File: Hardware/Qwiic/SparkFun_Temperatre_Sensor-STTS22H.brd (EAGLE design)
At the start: 25.4 x 25.4 mm, 54 parts, among them J1 QWIIC_RIGHT_ANGLE, J2 QWIIC_RIGHT_ANGLE, U2 STTS22H

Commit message: Moves OSHW logo, approves various DRC errors, moves silk
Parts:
- moved LOGO2 21.2 mm to (4.47, 5.95)
- moved U$6 3.18 mm to (17.8, 13.6)
- moved U$8 2.93 mm to (6.25, 13.7)
- moved U$19 0.13 mm to (16.6, 18.0)
- moved U$22 0.13 mm to (7.98, 18.0)
- moved U$25 0.13 mm to (12.7, 6.86)
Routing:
- net 3.3V: vias 5 -> 3
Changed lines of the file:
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@@
 <attribute name="REV" value="" x="-19.05" y="-16.51" size="1.778" layer="27" display="off"/>
 </element>
-<element name="LOGO2" library="SparkFun-Aesthetics" package="OSHW-LOGO-MINI" value="OSHW-LOGOMINI" x="23.7744" y="14.71295" smashed="yes" rot="MR0"/>
+<element name="LOGO2" library="SparkFun-Aesthetics" package="OSHW-LOGO-MINI" value="OSHW-LOGOMINI" x="4.4704" y="5.94995" smashed="yes" rot="MR0"/>
 <element name="STANDOFF1" library="SparkFun-Hardware" package="STAND-OFF-TIGHT" value="STAND-OFFTIGHT" x="2.54" y="22.86" smashed="yes"/>
 <element name="STANDOFF2" library="SparkFun-Hardware" package="STAND-OFF-TIGHT" value="STAND-OFFTIGHT" x="2.54" y="2.54" smashed="yes"/>
@@
 </element>
 <element name="U$16" library="bot" package="#LED#11" value="" x="23.622" y="16.9926" smashed="yes" rot="MR0"/>
-<element name="U$25" library="bot" package="#I2C#11" value="" x="12.7" y="6.985" smashed="yes" rot="MR0"/>
+<element name="U$25" library="bot" package="#I2C#11" value="" x="12.7" y="6.858" smashed="yes" rot="MR0"/>
 <element name="U$1" library="top" package="#GND#3" value="" x="7.62" y="3.937" smashed="yes" rot="R90"/>
 <element name="U$2" library="top" package="#3V3#4" value="" x="10.16" y="3.81" smashed="yes" rot="R90"/>
@@
 <attribute name="VALUE" value="15k" x="13.462" y="17.78" size="0.6096" layer="27" font="vector" ratio="20" rot="R90" align="top-center"/>
 </element>
-<element name="U$6" library="top" package="#ADDR#6" value="" x="17.78" y="16.8148" smashed="yes" rot="MR0"/>
+<element name="U$6" library="top" package="#ADDR#6" value="" x="17.78" y="13.6398" smashed="yes" rot="MR0"/>
 <element name="U2" library="STTS22H" package="UDFN-6L" value="STTS22H" x="12.7" y="12.7" smashed="yes">
 <attribute name="NAME" x="12.041" y="14.96833125" size="0.6096" layer="25" font="vector" ratio="20"/>
@@
 <element name="U$5" library="top" package="#SDA#7" value="" x="12.7" y="3.9116" smashed="yes" rot="MR270"/>
 <element name="U$7" library="top" package="#SCL#6" value="" x="15.24" y="3.7592" smashed="yes" rot="MR270"/>
-<element name="U$8" library="top" package="#ADDR1#9" value="" x="6.5024" y="16.5862" smashed="yes" rot="MR0"/>
+<element name="U$8" library="top" package="#ADDR1#9" value="" x="6.2484" y="13.6652" smashed="yes" rot="MR0"/>
 <element name="U$12" library="top" package="#0X3C#25" value="" x="14.4272" y="15.3416" smashed="yes" rot="MR0"/>
 <element name="U$13" library="top" package="#0X3E#25" value="" x="21.1836" y="15.3416" smashed="yes" rot="MR0"/>
@@
 <element name="U$15" library="top" package="#0X38#25" value="" x="3.2512" y="15.2908" smashed="yes" rot="MR0"/>
 <element name="U$17" library="top" package="TEMPERATURE23" value="" x="12.7" y="19.6088" smashed="yes" rot="MR0"/>
-<element name="U$19" library="top" package="SENSOR24" value="" x="16.6116" y="18.0848" smashed="yes" rot="MR0"/>
-<element name="U$22" library="top" package="STTS22H21" value="" x="7.9756" y="18.0848" smashed="yes" rot="MR0"/>
+<element name="U$19" library="top" package="SENSOR24" value="" x="16.6116" y="17.9578" smashed="yes" rot="MR0"/>
+<element name="U$22" library="top" package="STTS22H21" value="" x="7.9756" y="17.9578" smashed="yes" rot="MR0"/>
 <element name="U$23" library="top" package="TEMPERATURE23" value="" x="12.7" y="24.13" smashed="yes"/>
 <element name="U$24" library="top" package="SENSOR24" value="" x="12.7" y="22.5552" smashed="yes"/>
@@
 <wire x1="12.7" y1="6.985" x2="12.7" y2="8.382" width="0.4064" layer="16"/>
 <wire x1="10.16" y1="8.1534" x2="11.3284" y2="6.985" width="0.4064" layer="1"/>
-<via x="11.176" y="11.176" extent="1-16" drill="0.3048"/>
 <polygon width="0.127" layer="1" thermals="no">
 <vertex x="11.8364" y="11.938"/>
@@
 <wire x1="6.612" y1="13.2" x2="7.6572" y2="12.1548" width="0.4064" layer="1"/>
 <wire x1="15.24" y1="18.63" x2="12.7" y2="18.63" width="0.4064" layer="1"/>
-<via x="19.1596" y="12.2" extent="1-16" drill="0.3048"/>
 <wire x1="5.588" y1="15.1892" x2="5.5372" y2="15.24" width="0.4064" layer="16"/>
 <wire x1="5.08" y1="13.2" x2="3.945" y2="13.2" width="0.4064" layer="1"/>

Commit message: Moves address jumper for better symmetry
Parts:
- moved U$13 1.27 mm to (22.5, 15.3)
- moved U$12 1.27 mm to (15.7, 15.3)
- moved ADDR 1.27 mm to (19.1, 15.2)
- moved U$6 1.27 mm to (19.1, 13.6)
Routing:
- net ADDR: track 22.9 -> 25.3 mm
- net N$4: track 5.18 -> 6.32 mm
- net N$7: track 5.19 -> 6.22 mm
- net GND: vias 37 -> 39
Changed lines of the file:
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@@
 <setting verticaltext="up"/>
 </settings>
-<grid distance="0.05" unitdist="inch" unit="inch" style="dots" multiple="1" display="yes" altdistance="0.005" altunitdist="inch" altunit="inch"/>
+<grid distance="0.05" unitdist="inch" unit="inch" style="dots" multiple="1" display="yes" altdistance="0.001" altunitdist="inch" altunit="inch"/>
 <layers>
 <layer number="1" name="Top" color="4" fill="1" visible="yes" active="yes"/>
@@
 <attribute name="VALUE" x="6.35" y="-0.762" size="0.6096" layer="27" font="vector" ratio="20"/>
 </element>
-<element name="ADDR" library="SparkFun-Jumpers" package="SMT-JUMPER_3_1-NC_TRACE_SILK" package3d_urn="urn:adsk.eagle:package:39288/1" value="JUMPER-SMT_3_1-NC_TRACE_SILK" x="17.78" y="15.24" smashed="yes" rot="MR0">
-<attribute name="NAME" x="17.78" y="16.383" size="0.6096" layer="26" font="vector" ratio="20" rot="MR0" align="bottom-center"/>
-<attribute name="VALUE" x="17.78" y="14.097" size="0.6096" layer="28" font="vector" ratio="20" rot="MR0" align="top-center"/>
+<element name="ADDR" library="SparkFun-Jumpers" package="SMT-JUMPER_3_1-NC_TRACE_SILK" package3d_urn="urn:adsk.eagle:package:39288/1" value="JUMPER-SMT_3_1-NC_TRACE_SILK" x="19.05" y="15.24" smashed="yes" rot="MR0">
+<attribute name="NAME" x="19.05" y="16.383" size="0.6096" layer="26" font="vector" ratio="20" rot="MR0" align="bottom-center"/>
+<attribute name="VALUE" x="19.05" y="14.097" size="0.6096" layer="28" font="vector" ratio="20" rot="MR0" align="top-center"/>
 </element>
 <element name="R7" library="SparkFun-Resistors" package="0603" value="56k" x="15.24" y="17.78" smashed="yes" rot="R270">
@@
 <attribute name="VALUE" value="15k" x="13.462" y="17.78" size="0.6096" layer="27" font="vector" ratio="20" rot="R90" align="top-center"/>
 </element>
-<element name="U$6" library="top" package="#ADDR#6" value="" x="17.78" y="13.6398" smashed="yes" rot="MR0"/>
+<element name="U$6" library="top" package="#ADDR#6" value="" x="19.05" y="13.6398" smashed="yes" rot="MR0"/>
 <element name="U2" library="STTS22H" package="UDFN-6L" value="STTS22H" x="12.7" y="12.7" smashed="yes">
 <attribute name="NAME" x="12.041" y="14.96833125" size="0.6096" layer="25" font="vector" ratio="20"/>
@@
 <element name="U$7" library="top" package="#SCL#6" value="" x="15.24" y="3.7592" smashed="yes" rot="MR270"/>
 <element name="U$8" library="top" package="#ADDR1#9" value="" x="6.2484" y="13.6652" smashed="yes" rot="MR0"/>
-<element name="U$12" library="top" package="#0X3C#25" value="" x="14.4272" y="15.3416" smashed="yes" rot="MR0"/>
-<element name="U$13" library="top" package="#0X3E#25" value="" x="21.1836" y="15.3416" smashed="yes" rot="MR0"/>
+<element name="U$12" library="top" package="#0X3C#25" value="" x="15.6972" y="15.3416" smashed="yes" rot="MR0"/>
+<element name="U$13" library="top" package="#0X3E#25" value="" x="22.4536" y="15.3416" smashed="yes" rot="MR0"/>
 <element name="U$14" library="top" package="#0X3F#25" value="" x="9.5504" y="15.2908" smashed="yes" rot="MR0"/>
 <element name="U$15" library="top" package="#0X38#25" value="" x="3.2512" y="15.2908" smashed="yes" rot="MR0"/>
@@
 <via x="9.8044" y="5.8928" extent="1-16" drill="0.3048"/>
 <via x="17.9324" y="7.9756" extent="1-16" drill="0.3048"/>
-<via x="20.32" y="16.51" extent="1-16" drill="0.3048"/>
+<via x="20.1422" y="17.1704" extent="1-16" drill="0.3048"/>
 <contactref element="C1" pad="2"/>
 <via x="17.78" y="19.304" extent="1-16" drill="0.3048"/>
@@
 <via x="23.3172" y="11.0236" extent="1-16" drill="0.3048"/>
 <via x="13.716" y="17.3736" extent="1-16" drill="0.3048"/>
-<via x="16.51" y="17.653" extent="1-16" drill="0.3048"/>
-<via x="6.604" y="14.0462" extent="1-16" drill="0.3048"/>
+<via x="16.5354" y="17.7038" extent="1-16" drill="0.3048"/>
+<via x="8.1788" y="14.5542" extent="1-16" drill="0.3048"/>
+<via x="3.8608" y="14.224" extent="1-16" drill="0.3048"/>
+<via x="7.1628" y="16.6878" extent="1-16" drill="0.3048"/>
 </signal>
 <signal name="3.3V">
@@
 <wire x1="6.612" y1="13.2" x2="7.6572" y2="12.1548" width="0.4064" layer="1"/>
 <wire x1="15.24" y1="18.63" x2="12.7" y2="18.63" width="0.4064" layer="1"/>
-<wire x1="5.588" y1="15.1892" x2="5.5372" y2="15.24" width="0.4064" layer="16"/>
 <wire x1="5.08" y1="13.2" x2="3.945" y2="13.2" width="0.4064" layer="1"/>
 <wire x1="3.945" y1="13.2" x2="3.937" y2="13.208" width="0.4064" layer="1"/>
@@
 <contactref element="U2" pad="P2"/>
 <contactref element="R3" pad="1"/>
-<wire x1="9.375" y1="12.684" x2="9.359" y2="12.7" width="0.2032" layer="1"/>
 <wire x1="9.315" y1="12.744" x2="8.509" y2="13.55" width="0.2032" layer="1"/>
 <wire x1="8.509" y1="13.55" x2="7.5556" y2="13.55" width="0.2032" layer="1"/>
@@
 <contactref element="R8" pad="1"/>
 <wire x1="12.7" y1="16.93" x2="12.993" y2="16.637" width="0.2032" layer="1"/>
-<wire x1="12.993" y1="16.637" x2="13.97" y2="16.637" width="0.2032" layer="1"/>
-<via x="13.97" y="16.637" extent="1-16" drill="0.3048"/>
-<wire x1="13.97" y1="16.637" x2="13.97" y2="15.875" width="0.2032" layer="16"/>
-<wire x1="14.605" y1="15.24" x2="16.7386" y2="15.24" width="0.2032" layer="16"/>
-<wire x1="13.97" y1="15.875" x2="14.605" y2="15.24" width="0.2032" layer="16"/>
+<wire x1="12.993" y1="16.637" x2="13.7414" y2="16.637" width="0.2032" layer="1"/>
+<via x="13.7414" y="16.637" extent="1-16" drill="0.3048"/>
+<wire x1="13.7414" y1="16.637" x2="13.7414" y2="16.1036" width="0.2032" layer="16"/>
+<wire x1="14.605" y1="15.24" x2="18.0086" y2="15.24" width="0.2032" layer="16"/>
+<wire x1="13.7414" y1="16.1036" x2="14.605" y2="15.24" width="0.2032" layer="16"/>
 </signal>
 <signal name="N$7">
 <contactref element="ADDR" pad="1"/>
 <contactref element="R7" pad="2"/>
-<wire x1="18.9484" y1="15.367" x2="18.8214" y2="15.24" width="0.2032" layer="16"/>
 <wire x1="15.24" y1="16.93" x2="16.344" y2="16.93" width="0.2032" layer="1"/>
 <wire x1="16.344" y1="16.93" x2="16.383" y2="16.891" width="0.2032" layer="1"/>
 <via x="16.383" y="16.891" extent="1-16" drill="0.3048"/>
-<wire x1="16.383" y1="16.891" x2="18.415" y2="16.891" width="0.2032" layer="16"/>
-<wire x1="18.8214" y1="16.4846" x2="18.8214" y2="15.24" width="0.2032" layer="16"/>
-<wire x1="18.415" y1="16.891" x2="18.8214" y2="16.4846" width="0.2032" layer="16"/>
+<wire x1="19.589621875" y1="16.891" x2="16.383" y2="16.891" width="0.2032" layer="16"/>
+<wire x1="20.0914" y1="15.24" x2="20.0914" y2="16.389221875" width="0.2032" layer="16"/>
+<wire x1="20.0914" y1="16.389221875" x2="19.589621875" y2="16.891" width="0.2032" layer="16"/>
 </signal>
 <signal name="ADDR">
@@
 <wire x1="13.594" y1="12.065" x2="14.3336" y2="12.065" width="0.2032" layer="1"/>
 <via x="14.3336" y="12.065" extent="1-16" drill="0.3048"/>
-<wire x1="17.78" y1="12.7" x2="17.78" y2="15.24" width="0.2032" layer="16"/>
-<wire x1="14.3336" y1="12.065" x2="17.145" y2="12.065" width="0.2032" layer="16"/>
-<wire x1="17.145" y1="12.065" x2="17.78" y2="12.7" width="0.2032" layer="16"/>
-<wire x1="17.78" y1="15.24" x2="17.78" y2="16.256" width="0.2032" layer="16"/>
-<wire x1="17.78" y1="16.256" x2="17.653" y2="16.383" width="0.2032" layer="16"/>
-<wire x1="17.653" y1="16.383" x2="14.986" y2="16.383" width="0.2032" layer="16"/>
+<wire x1="18.6944" y1="16.383" x2="14.986" y2="16.383" width="0.2032" layer="16"/>
 <wire x1="14.986" y1="16.383" x2="14.605" y2="16.764" width="0.2032" layer="16"/>
 <wire x1="6.35" y1="17.145" x2="6.35" y2="15.24" width="0.2032" layer="16"/>
@@
 <wire x1="14.351" y1="17.907" x2="7.112" y2="17.907" width="0.2032" layer="16"/>
 <wire x1="7.112" y1="17.907" x2="6.35" y2="17.145" width="0.2032" layer="16"/>
+<wire x1="19.05" y1="16.0274" x2="19.05" y2="15.24" width="0.2032" layer="16"/>
+<wire x1="18.6944" y1="16.383" x2="19.05" y2="16.0274" width="0.2032" layer="16"/>
+<wire x1="18.4404" y1="12.065" x2="19.0627" y2="12.6873" width="0.2032" layer="16"/>
+<wire x1="14.3336" y1="12.065" x2="18.4404" y2="12.065" width="0.2032" layer="16"/>
+<wire x1="19.05" y1="15.24" x2="19.0627" y2="15.2273" width="0.2032" layer="16"/>
+<wire x1="19.0627" y1="15.2273" x2="19.0627" y2="12.6873" width="0.2032" layer="16"/>
 </signal>
 <signal name="SCL">
@@
 <contactref element="J2" pad="4"/>
 <contactref element="J3" pad="4"/>
-<wire x1="19.328" y1="14.2" x2="20.2946" y2="14.2" width="0.2032" layer="1"/>
+<wire x1="17.931" y1="14.2" x2="20.2946" y2="14.2" width="0.2032" layer="1"/>
 <wire x1="20.2946" y1="14.2" x2="21.487" y2="14.2" width="0.2032" layer="1"/>
 <wire x1="21.487" y1="14.2" x2="22.5298" y2="13.1572" width="0.2032" layer="1"/>
@@
 <wire x1="11.1252" y1="13.6652" x2="11.1252" y2="14.7828" width="0.2032" layer="1"/>
 <wire x1="11.1252" y1="14.7828" x2="10.7188" y2="15.1892" width="0.2032" layer="1"/>
-<wire x1="12.2936" y1="14.7828" x2="13.97" y2="14.7828" width="0.2032" layer="1"/>
-<wire x1="13.97" y1="14.7828" x2="18.7452" y2="14.7828" width="0.2032" layer="1"/>
-<wire x1="18.7452" y1="14.7828" x2="19.328" y2="14.2" width="0.2032" layer="1"/>
+<wire x1="12.2936" y1="14.7828" x2="17.3482" y2="14.7828" width="0.2032" layer="1"/>
+<wire x1="17.3482" y1="14.7828" x2="17.931" y2="14.2" width="0.2032" layer="1"/>
 <wire x1="10.7188" y1="15.1892" x2="9.8552" y2="15.1892" width="0.2032" layer="1"/>
 <wire x1="9.315" y1="15.7294" x2="9.315" y2="16.6946" width="0.2032" layer="1"/>

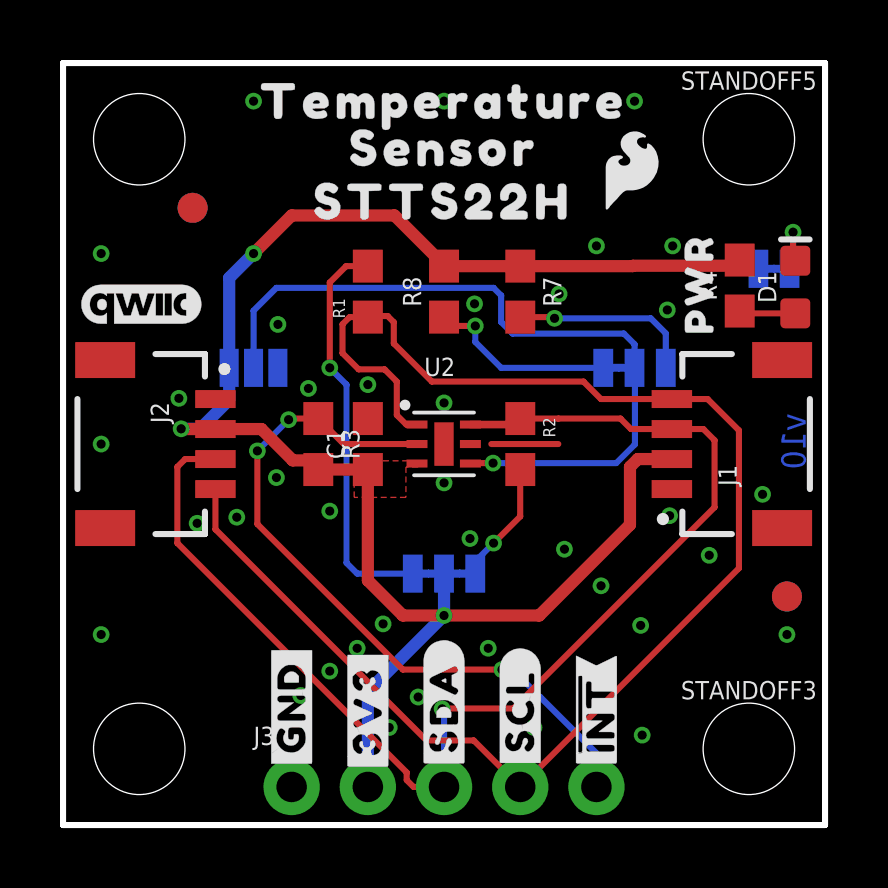
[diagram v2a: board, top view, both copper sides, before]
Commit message: Adds a single, incredibly important via
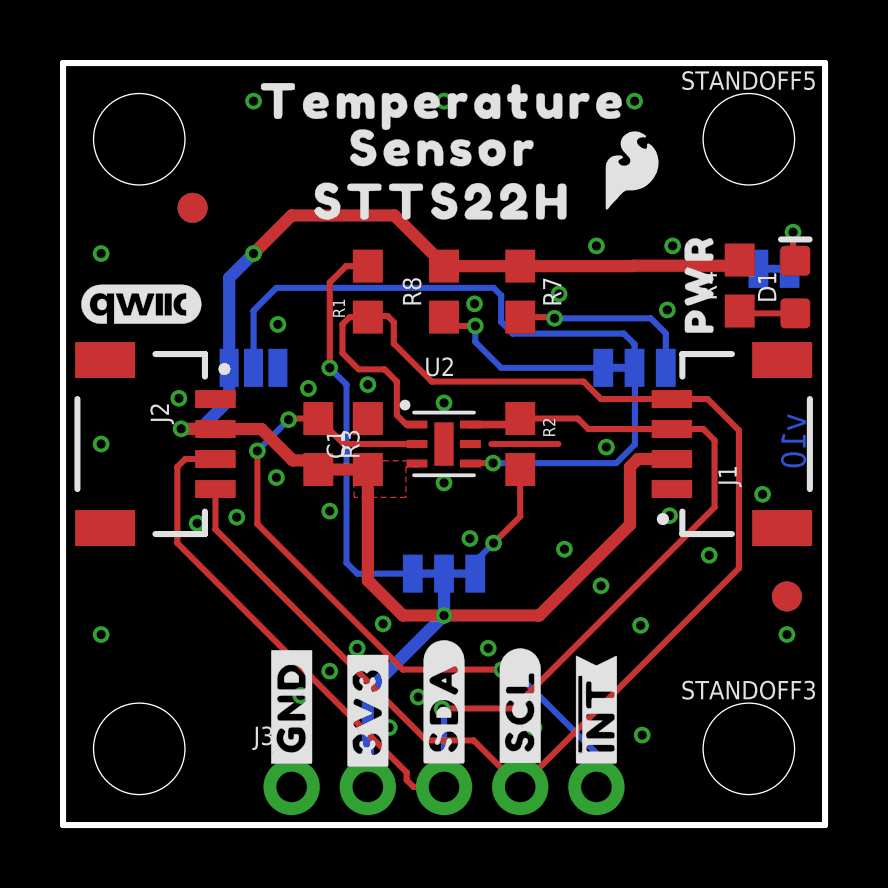
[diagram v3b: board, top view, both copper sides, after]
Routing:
- net GND: vias 39 -> 40
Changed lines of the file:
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@@
 <via x="3.8608" y="14.224" extent="1-16" drill="0.3048"/>
 <via x="7.1628" y="16.6878" extent="1-16" drill="0.3048"/>
+<via x="18.1102" y="12.5984" extent="1-16" drill="0.3048"/>
 </signal>
 <signal name="3.3V">
@@
 <wire x1="4.072" y1="12.2" x2="5.08" y2="12.2" width="0.2032" layer="1"/>
 <wire x1="3.81" y1="11.938" x2="4.072" y2="12.2" width="0.2032" layer="1"/>
-<wire x1="15.24" y1="13.55" x2="16.51" y2="13.55" width="0.2032" layer="1"/>
-<wire x1="16.51" y1="13.55" x2="18.581" y2="13.55" width="0.2032" layer="1"/>
-<wire x1="18.931" y1="13.2" x2="20.2946" y2="13.2" width="0.2032" layer="1"/>
-<wire x1="18.581" y1="13.55" x2="18.931" y2="13.2" width="0.2032" layer="1"/>
+<wire x1="15.24" y1="13.55" x2="17.1586" y2="13.55" width="0.2032" layer="1"/>
+<wire x1="17.5086" y1="13.2" x2="20.2946" y2="13.2" width="0.2032" layer="1"/>
+<wire x1="17.1586" y1="13.55" x2="17.5086" y2="13.2" width="0.2032" layer="1"/>
 <wire x1="15.455" y1="13.55" x2="15.24" y2="13.55" width="0.2032" layer="1"/>
 <wire x1="15.239" y1="13.334" x2="15.455" y2="13.55" width="0.2032" layer="1"/>
